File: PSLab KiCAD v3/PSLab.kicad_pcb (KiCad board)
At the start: 4 copper layers, 72.9 x 53.6 mm, 141 parts, among them CON1 USB-MINI-B, J1 V+, J2 GND, J3 V-, J4 Expansion, J5 PG_Pins, J6 Exp, J7 VR-, J8 ESPROG, J9 VR+, P1 CONN_01X08, P10 Analog, P3 DIO, P5 sen-cap, P6 I2C, P7 NRF, P9 Tx-Rx, Q1 3906, U1 MCP2200, U10 TL082, U11 6S21, U12 6S21, U13 TL082, U15 ESP8266, U16 TL082, U2 74HC126, U3 PIC24EP64GP204, U4 TC1240A, U5 7660, U6 LM1117-3.3, U7 LM324, U8 TL082, U9 MCP4728, X1 12MHz

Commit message: Labeling the PCB
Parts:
- added REF***: ESD-Logo_6.6x6mm_SilkScreen, Symbols:ESD-Logo_6.6x6mm_SilkScreen, F.Cu at (119.3, 120.2)
- C14, C16, C19: moved to F.Cu
- U4: moved to B.Cu
- moved C16 26.8 mm to (156.7, 78.0), turned to 180 degrees
- moved R4 4.91 mm to (132.3, 112.1), turned to 90 degrees
- moved R13 3.54 mm to (126.5, 113.2)
- moved C19 3.28 mm to (124.2, 120.7)
- moved C21 2.67 mm to (149.8, 79.5), turned to 0 degrees
- moved C26 2.22 mm to (153.2, 82.1)
- moved C6 2.09 mm to (126.5, 116.5)
- moved J3 1.71 mm to (124.2, 122.1)
- moved U4 1.64 mm to (133.7, 89.5)
- moved R5 1.49 mm to (173.9, 106.8)
- moved C9 1.37 mm to (147.2, 104.1)
- moved R17 1.19 mm to (173.3, 102.3)
- moved R11 1.02 mm to (125.5, 119.5)
- moved R35 0.91 mm to (165.3, 109.0)
- moved R21 0.81 mm to (179.3, 110.8)
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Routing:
- net Net-(C16-Pad1): track 6.13 -> 33.4 mm, vias 1 -> 3
- net GND: track 508.4 -> 534.8 mm
- net Net-(C16-Pad2): track 4.70 -> 28.9 mm, vias 1 -> 3
- net +5V: track 85.5 -> 95.6 mm, vias 4 -> 6
- net V-: track 97.9 -> 91.2 mm, vias 6 -> 4
- net Net-(C11-Pad1): track 26.4 -> 30.9 mm, vias 1 -> 3
- net Net-(C40-Pad1): track 44.4 -> 47.5 mm
- net SQ4: track 32.2 -> 35.3 mm
- net Net-(C14-Pad2): track 3.78 -> 6.67 mm
- net /SEN: track 28.2 -> 31.0 mm
- net AN4: track 25.6 -> 28.1 mm
- net Net-(C18-Pad2): track 26.2 -> 28.7 mm
- net V+: track 91.3 -> 88.9 mm, vias 6 -> 5
- net VR+: track 65.1 -> 67.2 mm
- net AVdd: track 140.0 -> 142.0 mm
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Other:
- net class Default: clearance 0.1032 -> 0.156
- rule trace_clearance: 0.1032 -> 0.156
- rule via_min_size: 0.8636 -> 0.3
- board text added: "+5V PGD PGC RP41"
- board text added: "AC1 GND CH1 GND CH2 GND CH3 GND"
- board text added: "AN4 SDI CE2 VDD"
- board text added: "AN8 VDD"
- board text added: "ESP8266"
- board text added: "ESPROG"
- board text added: "GND SQ1 SQ2 SQ3 SQ4 FCi ID1 ID2 ID3 ID4"
- board text added: "MCLR GND"
- board text added: "PSLab by FOSSASIA"
- board text added: "PV1 PV2 PV3 PCS GND SI1 GND SI2"
- board text added: "SCL GND"
- board text added: "SDA VDD"
- board text added: "SDI SDO SCK"
- board text added: "SDO SCK CE1 GND"
- board text added: "SEN GND CAP MIC GND C3G"
- board text added: "TX RX"
- board text added: "pslab.fossasia.org"

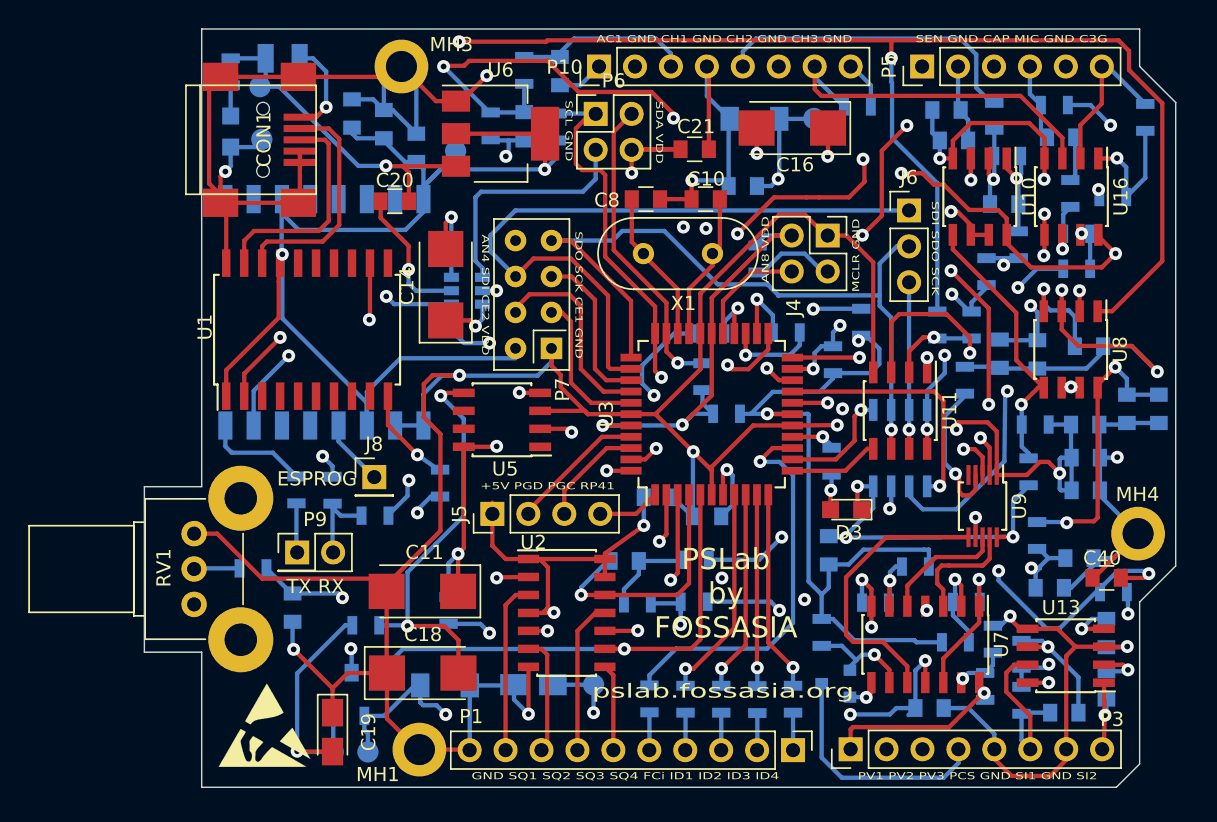
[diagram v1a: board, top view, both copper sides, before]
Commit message: Adding zones
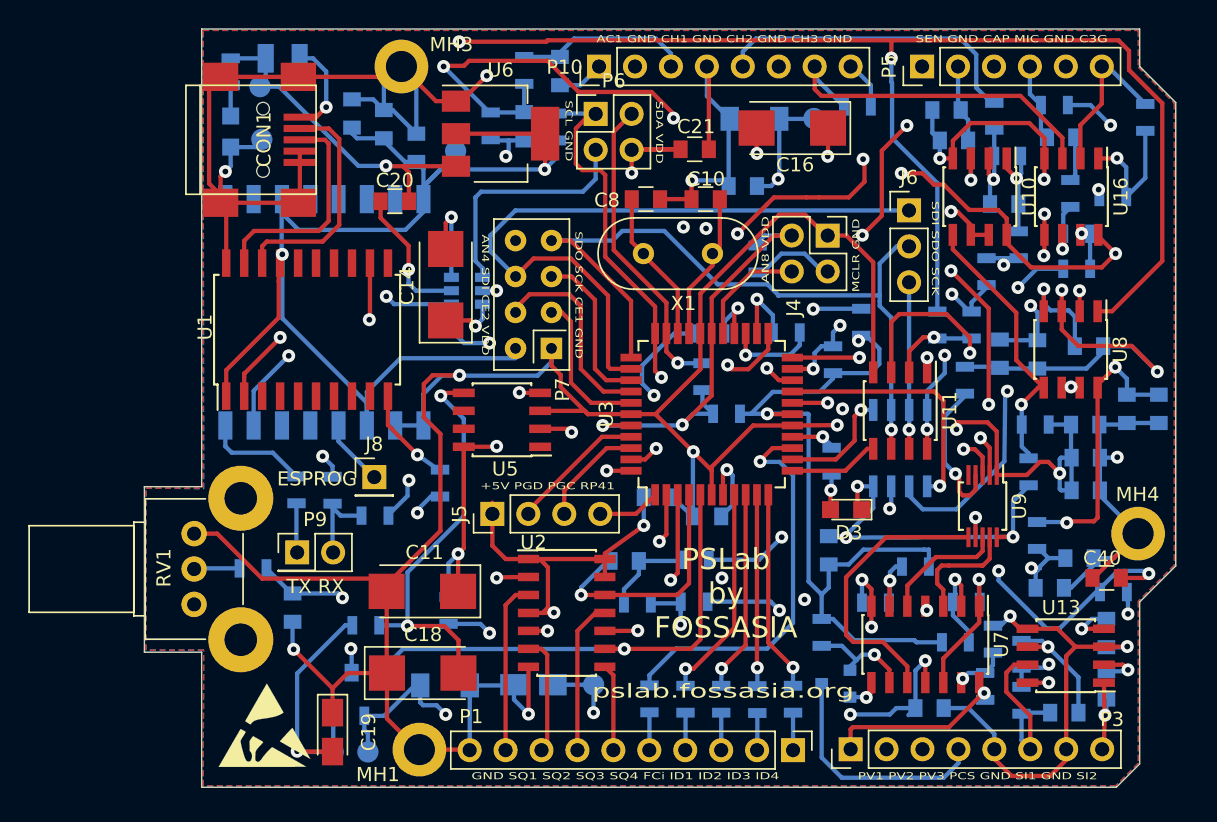
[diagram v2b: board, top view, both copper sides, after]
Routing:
- added copper zone on F.Cu, net (none)
- added copper zone on B.Cu, net GND
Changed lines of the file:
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@@
     (user_trace_width 1.27)
     (trace_clearance 0.156)
-    (zone_clearance 0.508)
+    (zone_clearance 0.6)
     (zone_45_only no)
     (trace_min 0.254)
@@
   (segment (start 149.1 119.325) (end 149.1 121.955) (width 0.3048) (layer B.Cu-L4) (net 112))
   (segment (start 149.1 121.955) (end 149.08 121.975) (width 0.3048) (layer B.Cu-L4) (net 112))
+  (zone (net 1) (net_name GND) (layer B.Cu-L4) (hatch edge 0.508)
+    (connect_pads (clearance 0.6))
+    (min_thickness 0.3)
+    (fill yes (arc_segments 16) (thermal_gap 0.508) (thermal_bridge_width 0.508))
+    (polygon
+      (pts
+        (xy 115 71.1) (xy 181.1 71.1) (xy 181.1 73.7) (xy 183.65 76.25) (xy 183.65 108.9)
+        (xy 181.1 111.45) (xy 181.1 122.9) (xy 179.5 124.5) (xy 115 124.5) (xy 115.05 114.9)
+        (xy 110.95 114.9) (xy 110.95 103.45) (xy 115.05 103.5)
+      )
+    )
+  )
+  (zone (net 0) (net_name "") (layer F.Cu-L1) (hatch edge 0.508)
+    (connect_pads (clearance 0.6))
+    (min_thickness 0.3)
+    (fill yes (arc_segments 16) (thermal_gap 0.508) (thermal_bridge_width 0.508))
+    (polygon
+      (pts
+        (xy 181.1 73.7) (xy 183.65 76.25) (xy 183.65 108.9) (xy 181.1 111.45) (xy 181.1 122.9)
+        (xy 179.5 124.5) (xy 115 124.5) (xy 115.05 114.9) (xy 110.95 114.9) (xy 110.95 103.45)
+        (xy 115 103.45) (xy 115 71.1) (xy 181.1 71.1)
+      )
+    )
+  )
 )

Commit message: Fixes #23 : Replaced USB port with USB Micro B type (#24)
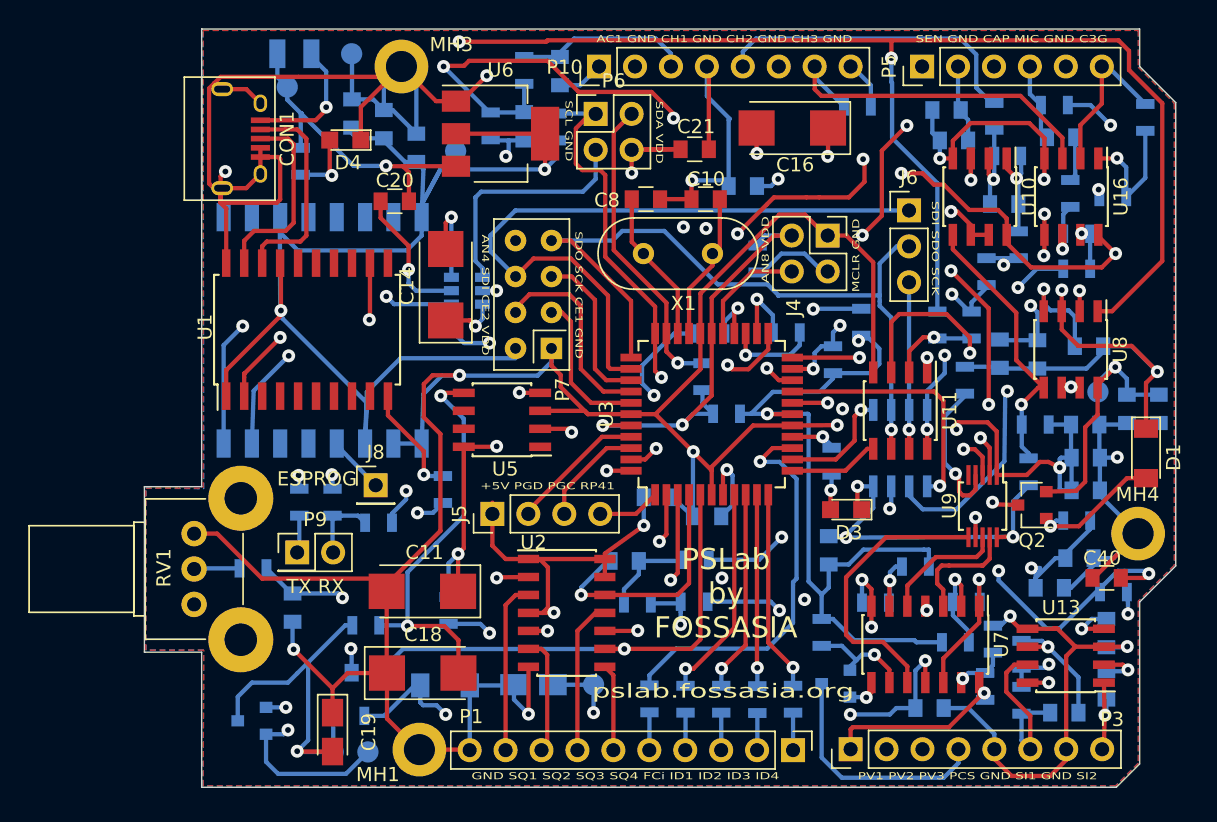
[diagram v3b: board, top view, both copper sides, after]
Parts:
- removed REF***: ESD-Logo_6.6x6mm_SilkScreen, Symbols:ESD-Logo_6.6x6mm_SilkScreen
- added Q2: MMBT3904, TO_SOT_Packages_SMD:SOT-23, F.Cu at (173.6, 104.7)
- added Q3: MMBT3906, TO_SOT_Packages_SMD:SOT-23, B.Cu at (118.5, 119.9)
- CON1: footprint Connectors:USB_Mini-B -> Connectors:USB_Micro-B
- D1: value 5V6 -> 6V8; moved to F.Cu
- D2: value 5V6 -> 6V8
- D4: moved to F.Cu
- R11, R5: value 200 -> 1K
- moved D1 36.4 mm to (181.7, 101.0), turned to 270 degrees
- moved J9 27.9 mm to (178.2, 96.7)
- moved J2 8.77 mm to (125.5, 72.8)
- moved D4 8.12 mm to (125.0, 78.8), turned to 180 degrees
- moved R53 8.03 mm to (121.9, 80.3)
- moved R5 2.99 mm to (176.8, 105.8), turned to 180 degrees
- moved TP1 1.93 mm to (121.0, 75.1)
- moved CON1 1.34 mm to (117.7, 78.8), turned to 270 degrees
- moved U15 1.28 mm to (123.5, 92.3)
- moved R57 0.90 mm to (121.8, 104.5)
- moved F1 0.89 mm to (121.5, 72.8)
- moved R56 0.85 mm to (124.2, 104.5)
- moved J8 0.58 mm to (127.2, 103.2)
- moved R54 0.56 mm to (127.4, 105.9)
- moved R55 0.49 mm to (131.9, 103.5)
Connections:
- D1 pad 2: VR+ -> Net-(D1-Pad2)
- D2 pad 1: VR- -> Net-(D2-Pad1)
- R11 pad 1: VR- -> Net-(D2-Pad1)
- R5 pad 1: VR+ -> V+
- R5 pad 2: V+ -> Net-(D1-Pad2)
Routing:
- net Net-(D2-Pad1): track 0.00 -> 21.4 mm, vias 0 -> 2
- net GND: track 534.8 -> 553.9 mm
- net /ETxD: track 7.38 -> 22.5 mm, vias 0 -> 2
- net Net-(D1-Pad2): track 0.00 -> 10.0 mm, vias 0 -> 1
- net V+: track 88.9 -> 96.8 mm, vias 5 -> 6
- net VR+: track 67.2 -> 59.2 mm, vias 5 -> 4
- net VR-: track 130.6 -> 122.8 mm
- net V-: track 91.2 -> 98.2 mm
- net Vdd: track 188.4 -> 194.9 mm
- net Net-(D4-Pad2): track 2.18 -> 4.78 mm, vias 0 -> 1
- net Net-(CON1-Pad1): track 6.94 -> 9.32 mm
- net /ERxD: track 15.8 -> 17.9 mm
- net /D+: track 15.8 -> 13.7 mm
- net /D-: track 16.4 -> 15.0 mm
- net /MTxD: track 6.94 -> 8.12 mm
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
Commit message: Added Gerber files
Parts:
- removed P6: I2C, Pin_Headers:Pin_Header_Straight_2x02_Pitch2.54mm
- removed P9: Tx-Rx, Pin_Headers:Pin_Header_Straight_2x01_Pitch2.54mm
- added J10: I2C-I, Pin_Headers:Pin_Header_Straight_1x02_Pitch2.54mm, F.Cu at (142.8, 77.0)
- added J11: I2C-II, Pin_Headers:Pin_Header_Straight_1x02_Pitch2.54mm, F.Cu at (145.3, 79.7)
- added J12: Ex-II, Pin_Headers:Pin_Header_Straight_1x02_Pitch2.54mm, F.Cu at (156.7, 85.6)
- C12, C19: footprint Capacitors_Tantalum_SMD:CP_Tantalum_Case-A_EIA-3216-18_Reflow -> Capacitors_Tantalum_SMD:CP_Tantalum_Case-B_EIA-3528-21_Reflow
- C21: value 1u -> 10u
- CON1: value USB-MINI-B -> USB-MICRO-B
- J4: value Expansion -> Ex-I; footprint Pin_Headers:Pin_Header_Straight_2x02_Pitch2.54mm -> Pin_Headers:Pin_Header_Straight_1x02_Pitch2.54mm
- J8: value ESPROG -> TX_RX_ES; footprint Pin_Headers:Pin_Header_Straight_1x01_Pitch2.54mm -> Pin_Headers:Pin_Header_Straight_1x03_Pitch2.54mm
- Q1: value 3906 -> MMBT3906; moved to F.Cu
- moved J8 4.47 mm to (126.8, 107.7), turned to 270 degrees
- moved C32 3.40 mm to (163.3, 117.4), turned to 270 degrees
- moved Q1 2.02 mm to (157.8, 117.7)
- moved R26 1.75 mm to (168.7, 118.1), turned to 0 degrees
- moved R5 1.31 mm to (175.4, 105.9)
- moved TP2 1.22 mm to (132.8, 78.4)
- moved R54 1.20 mm to (127.3, 104.7)
- moved C21 0.92 mm to (149.6, 78.6), turned to 90 degrees
- moved C15 0.76 mm to (150.3, 106.2)
- moved R32 0.65 mm to (162.2, 91.9)
- moved R52 0.46 mm to (159.3, 102.0)
- moved R41 0.36 mm to (173.2, 115.0)
- moved R18 0.34 mm to (167.9, 114.1)
- moved R1 0.26 mm to (154.2, 87.0)
- moved X1 0.22 mm to (146.2, 86.7)
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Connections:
- R36 pad 2: Net-(Q1-Pad1) -> Net-(Q1-Pad2)
- U7 pad 8: Net-(Q1-Pad2) -> Net-(Q1-Pad1)
- U7 pad 9: Net-(Q1-Pad1) -> Net-(Q1-Pad2)
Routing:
- net +5V: track 95.9 -> 117.6 mm
- net PVS3: track 20.2 -> 32.8 mm
- net GND: track 553.9 -> 545.6 mm, vias 21 -> 20
- net 12MHz: track 44.3 -> 52.6 mm
- net AVdd: track 141.8 -> 149.8 mm, vias 9 -> 10
- net Net-(R25-Pad2): track 3.74 -> 11.0 mm
- net Net-(Q1-Pad2): track 2.36 -> 9.19 mm
- net Net-(CON1-Pad1): track 9.32 -> 14.8 mm
- net /ESPROG: track 4.06 -> 8.74 mm, vias 0 -> 1
- net Net-(D1-Pad2): track 10.0 -> 14.1 mm
- net /RxD: track 34.1 -> 37.7 mm
- net /CAP: track 33.3 -> 37.0 mm
- net PVS2: track 14.3 -> 17.9 mm
- net Net-(Q1-Pad1): track 7.62 -> 4.09 mm, vias 1 -> 0
- net PVS1: track 13.9 -> 16.8 mm
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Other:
- board text added: "Rev 2 @ 15Dec17"
- board text added: "SCL VDD"
- board text added: "SDA GND"
- board text added: "TX RX ESP"
- board text removed: "ESPROG"
- board text removed: "SCL GND"
- board text removed: "SDA VDD"
- board text removed: "TX RX"

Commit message: Fixes #27 : Replaced microcontroller
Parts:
- U3: value PIC24EP64GP204 -> PIC24EP256GP204
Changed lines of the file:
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@@
     (links 339)
     (no_connects 0)
-    (area 102.332999 70.5864 183.800001 127.09)
+    (area 110.799999 70.949999 183.800001 124.650001)
     (thickness 1.6)
     (drawings 32)
@@
       (effects (font (size 1 1) (thickness 0.15)))
     )
-    (fp_text value PIC24EP64GP204 (at 0 7.45 90) (layer F.Fab)
+    (fp_text value PIC24EP256GP204 (at 0 7.45 90) (layer F.Fab)
       (effects (font (size 1 1) (thickness 0.15)))
     )
